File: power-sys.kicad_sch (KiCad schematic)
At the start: 25 parts, among them J1 Conn_01x02, J15 USB_C_Receptacle_USB2.0_14P, SW3 SW_SPST, U2 MCP73831-2-OT, U4 LM66200DRLR, U5 RT9080-33GJ5, U6 TPS61022

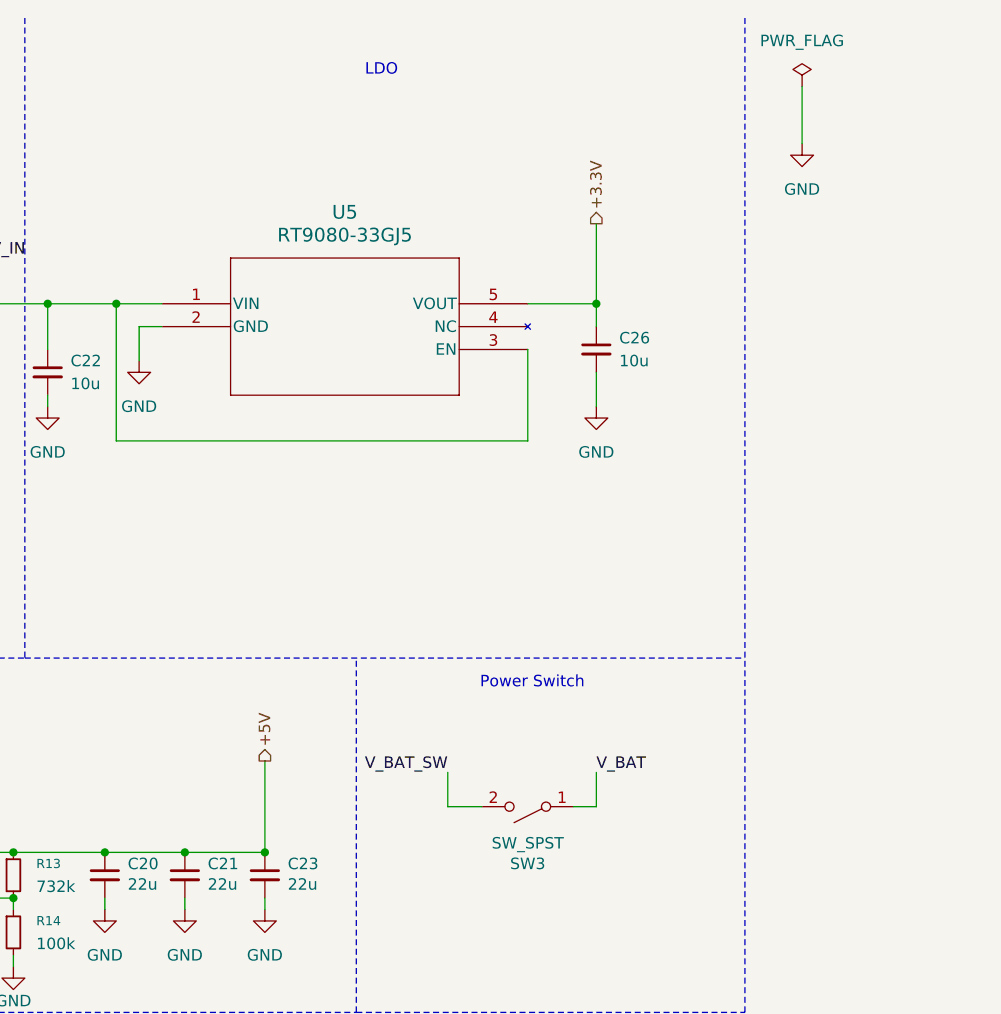
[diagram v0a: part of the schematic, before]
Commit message: Add testpoints
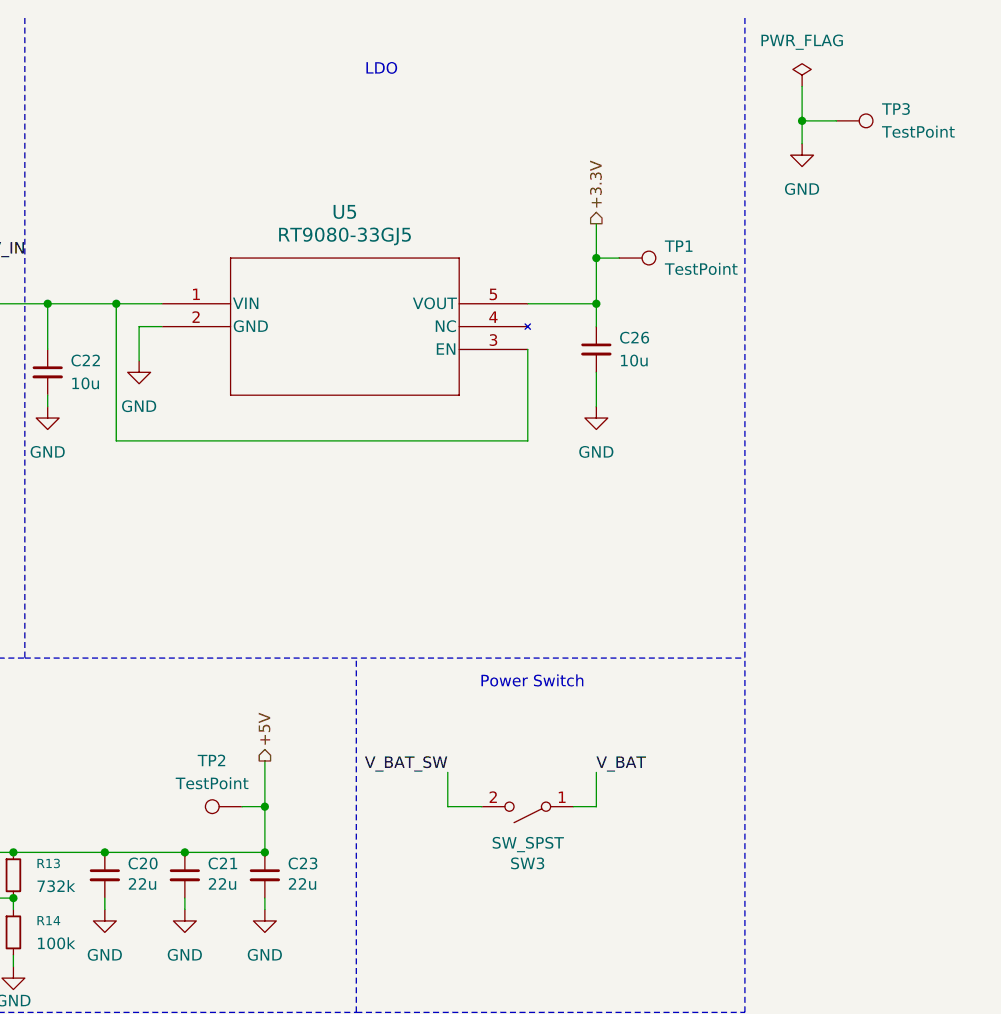
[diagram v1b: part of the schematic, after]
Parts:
- added TP1, TP2, TP3: TestPoint, TestPoint:TestPoint_THTPad_D1.5mm_Drill0.7mm, symbol Connector:TestPoint
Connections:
- net +3.3V: now also TP1.1
- net +5V: now also TP2.1
- net GND: now also TP3.1

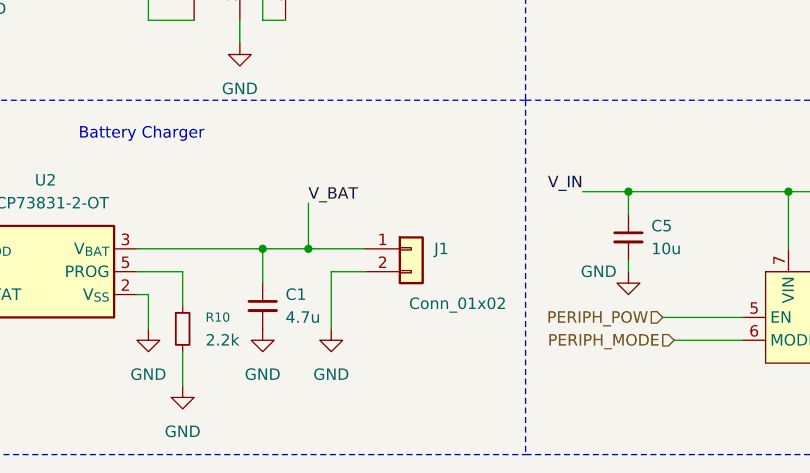
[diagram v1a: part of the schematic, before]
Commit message: Fix some bugs in the circuit
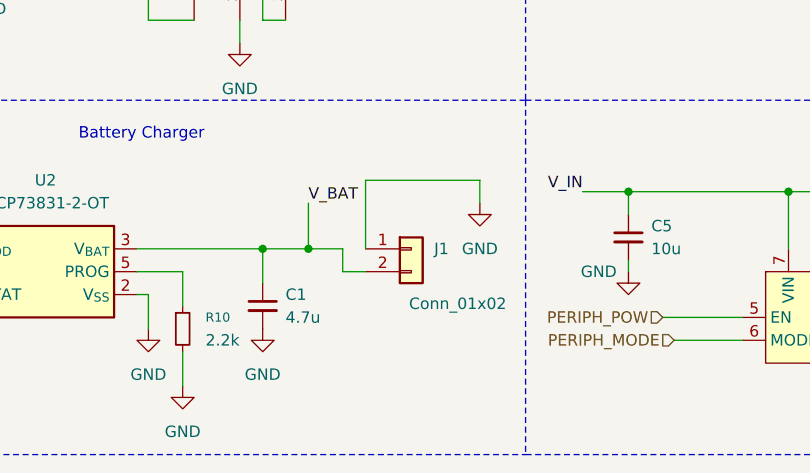
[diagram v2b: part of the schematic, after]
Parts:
- J1: footprint Connector_JST:JST_XH_S2B-XH-A-1_1x02_P2.50mm_Horizontal -> Connector_JST:JST_PH_S2B-PH-K_1x02_P2.00mm_Horizontal
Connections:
- net GND: now also J1.1 (Pin_1); no longer J1.2 (Pin_2)
- net V_BAT: now also J1.2 (Pin_2); no longer J1.1 (Pin_1)
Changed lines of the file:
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@@
 	(wire
 		(pts
-			(xy 71.12 100.33) (xy 77.47 100.33)
+			(xy 71.12 100.33) (xy 74.93 100.33)
 		)
 		(stroke
@@
 	(wire
 		(pts
+			(xy 74.93 102.87) (xy 74.93 100.33)
+		)
+		(stroke
+			(width 0)
+			(type default)
+		)
+	)
+	(wire
+		(pts
 			(xy 158.75 116.84) (xy 158.75 118.11)
 		)
@@
 	(wire
 		(pts
-			(xy 77.47 102.87) (xy 73.66 102.87)
+			(xy 132.08 93.98) (xy 134.62 93.98)
 		)
 		(stroke
@@
 	(wire
 		(pts
-			(xy 132.08 93.98) (xy 134.62 93.98)
+			(xy 77.47 102.87) (xy 74.93 102.87)
 		)
 		(stroke
@@
 	(wire
 		(pts
+			(xy 77.47 100.33) (xy 77.47 92.71)
+		)
+		(stroke
+			(width 0)
+			(type default)
+		)
+	)
+	(wire
+		(pts
 			(xy 162.56 44.45) (xy 170.18 44.45)
 		)
@@
 	(wire
 		(pts
-			(xy 27.94 73.66) (xy 27.94 76.2)
+			(xy 77.47 92.71) (xy 90.17 92.71)
 		)
 		(stroke
@@
 	(wire
 		(pts
-			(xy 53.34 39.37) (xy 53.34 74.93)
+			(xy 27.94 73.66) (xy 27.94 76.2)
 		)
 		(stroke
@@
 	(wire
 		(pts
-			(xy 50.8 34.29) (xy 78.74 34.29)
+			(xy 53.34 39.37) (xy 53.34 74.93)
 		)
 		(stroke
@@
 	(wire
 		(pts
-			(xy 162.56 54.61) (xy 162.56 55.88)
+			(xy 50.8 34.29) (xy 78.74 34.29)
 		)
 		(stroke
@@
 	(wire
 		(pts
-			(xy 73.66 102.87) (xy 73.66 109.22)
+			(xy 162.56 54.61) (xy 162.56 55.88)
 		)
 		(stroke
@@
 	(wire
 		(pts
+			(xy 90.17 92.71) (xy 90.17 95.25)
+		)
+		(stroke
+			(width 0)
+			(type default)
+		)
+	)
+	(wire
+		(pts
 			(xy 246.38 20.32) (xy 246.38 24.13)
 		)
@@
 			)
 		)
-		(property "Footprint" "Connector_JST:JST_XH_S2B-XH-A-1_1x02_P2.50mm_Horizontal"
+		(property "Footprint" "Connector_JST:JST_PH_S2B-PH-K_1x02_P2.00mm_Horizontal"
 			(at 82.55 100.33 0)
 			(hide yes)
@@
 	)
 	(symbol
-		(lib_id "power:GND")
-		(at 73.66 109.22 0)
-		(unit 1)
-		(body_style 1)
-		(exclude_from_sim no)
-		(in_bom yes)
-		(on_board yes)
-		(in_pos_files yes)
-		(dnp no)
-		(fields_autoplaced yes)
-		(property "Reference" "#PWR0128"
-			(at 73.66 115.57 0)
-			(hide yes)
-			(show_name no)
-			(do_not_autoplace no)
-			(effects
-				(font
-					(size 1.27 1.27)
-				)
-			)
-		)
-		(property "Value" "GND"
-			(at 73.66 114.3 0)
-			(show_name no)
-			(do_not_autoplace no)
-			(effects
-				(font
-					(size 1.27 1.27)
-				)
-			)
-		)
-		(property "Footprint" ""
-			(at 73.66 109.22 0)
-			(hide yes)
-			(show_name no)
-			(do_not_autoplace no)
-			(effects
-				(font
-					(size 1.27 1.27)
-				)
-			)
-		)
-		(property "Datasheet" ""
-			(at 73.66 109.22 0)
-			(hide yes)
-			(show_name no)
-			(do_not_autoplace no)
-			(effects
-				(font
-					(size 1.27 1.27)
-				)
-			)
-		)
-		(property "Description" "Power symbol creates a global label with name \"GND\" , ground"
-			(at 73.66 109.22 0)
-			(hide yes)
-			(show_name no)
-			(do_not_autoplace no)
-			(effects
-				(font
-					(size 1.27 1.27)
-				)
-			)
-		)
-		(pin "1"
-		)
-		(instances
-			(project "octov1.1"
-				(path "/24892b13-7569-4118-b17c-686e889722f8/55bb895a-3850-4b6e-addb-0e9f4b6de5dd"
-					(reference "#PWR0128")
-					(unit 1)
-				)
-			)
-		)
-	)
-	(symbol
 		(lib_id "Connector:USB_C_Receptacle_USB2.0_14P")
 		(at 35.56 41.91 0)
@@
 					(unit 1)
 				)
+			)
+		)
+	)
+	(symbol
+		(lib_id "power:GND")
+		(at 90.17 95.25 0)
+		(unit 1)
+		(body_style 1)
+		(exclude_from_sim no)
+		(in_bom yes)
+		(on_board yes)
+		(in_pos_files yes)
+		(dnp no)
+		(fields_autoplaced yes)
+		(property "Reference" "#PWR03"
+			(at 90.17 101.6 0)
+			(hide yes)
+			(show_name no)
+			(do_not_autoplace no)
+			(effects
+				(font
+					(size 1.27 1.27)
+				)
+			)
+		)
+		(property "Value" "GND"
+			(at 90.17 100.33 0)
+			(show_name no)
+			(do_not_autoplace no)
+			(effects
+				(font
+					(size 1.27 1.27)
+				)
+			)
+		)
+		(property "Footprint" ""
+			(at 90.17 95.25 0)
+			(hide yes)
+			(show_name no)
+			(do_not_autoplace no)
+			(effects
+				(font
+					(size 1.27 1.27)
+				)
+			)
+		)
+		(property "Datasheet" ""
+			(at 90.17 95.25 0)
+			(hide yes)
+			(show_name no)
+			(do_not_autoplace no)
+			(effects
+				(font
+					(size 1.27 1.27)
+				)
+			)
+		)
+		(property "Description" "Power symbol creates a global label with name \"GND\" , ground"
+			(at 90.17 95.25 0)
+			(hide yes)
+			(show_name no)
+			(do_not_autoplace no)
+			(effects
+				(font
+					(size 1.27 1.27)
+				)
+			)
+		)
+		(pin "1"
+		)
+		(instances
+			(project "octov1.1"
+				(path "/24892b13-7569-4118-b17c-686e889722f8/55bb895a-3850-4b6e-addb-0e9f4b6de5dd"
+					(reference "#PWR03")
+					(unit 1)
+				)
